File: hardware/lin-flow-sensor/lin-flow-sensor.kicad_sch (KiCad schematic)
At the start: 27 parts, among them J1 UPDI, J2 I2C LCD, J3 Screw_Terminal_01x03, Q1 2N7002, Q2 2N7002, U1 TJA1021T, U2 ATtiny824-X, U3 PCA9536DP

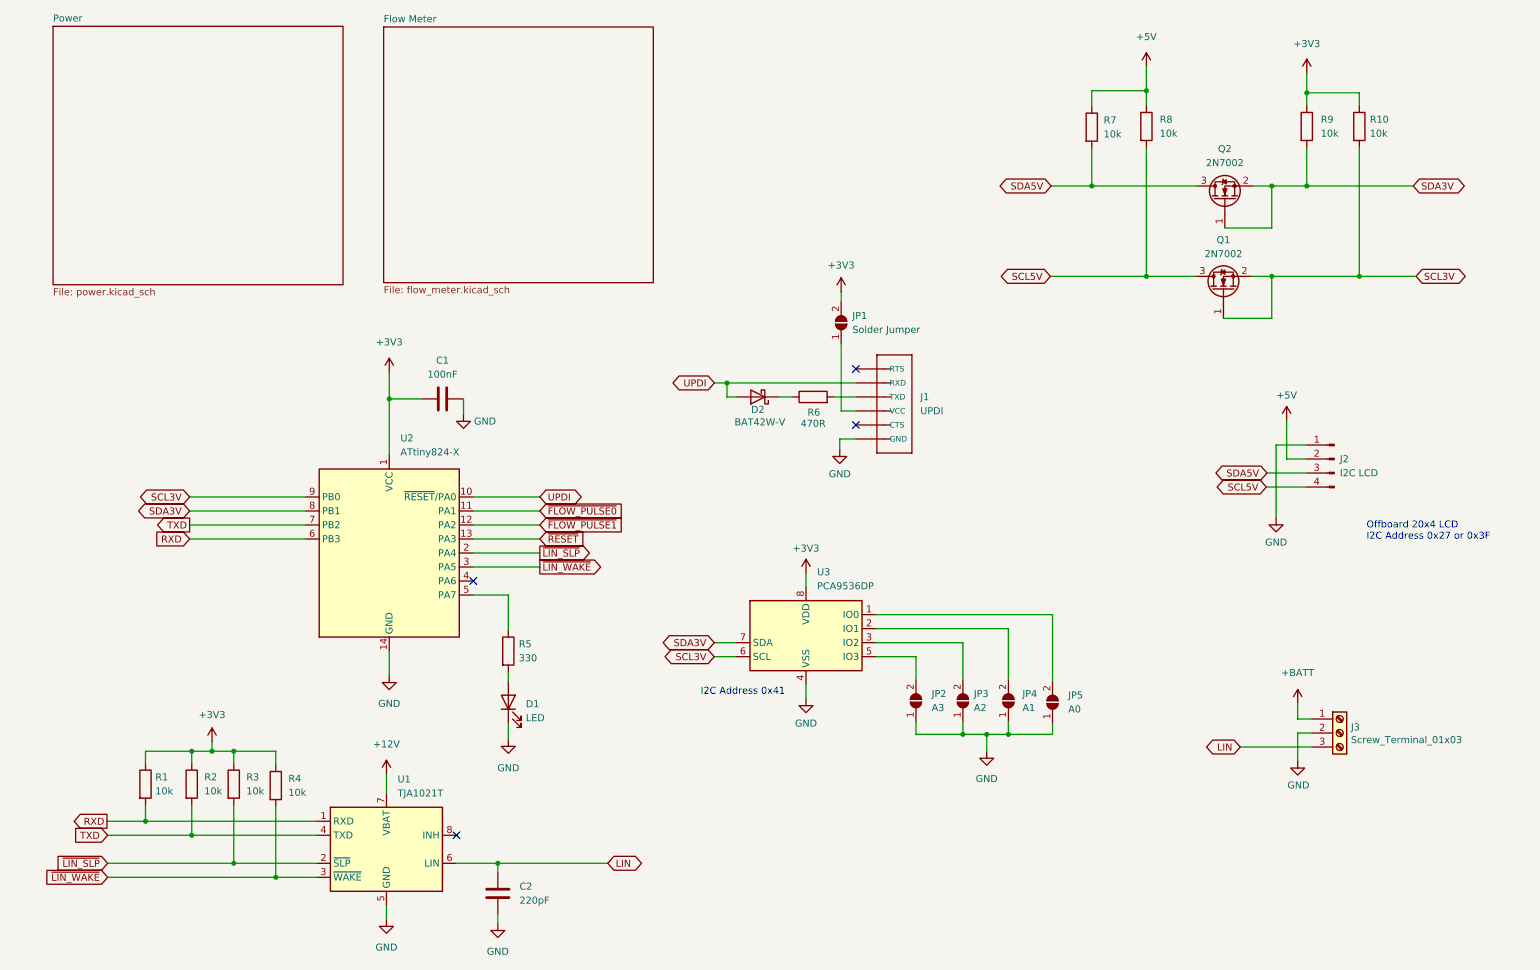
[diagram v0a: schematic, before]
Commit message: Update the schematics... remove PCA9536, use voltage regulator
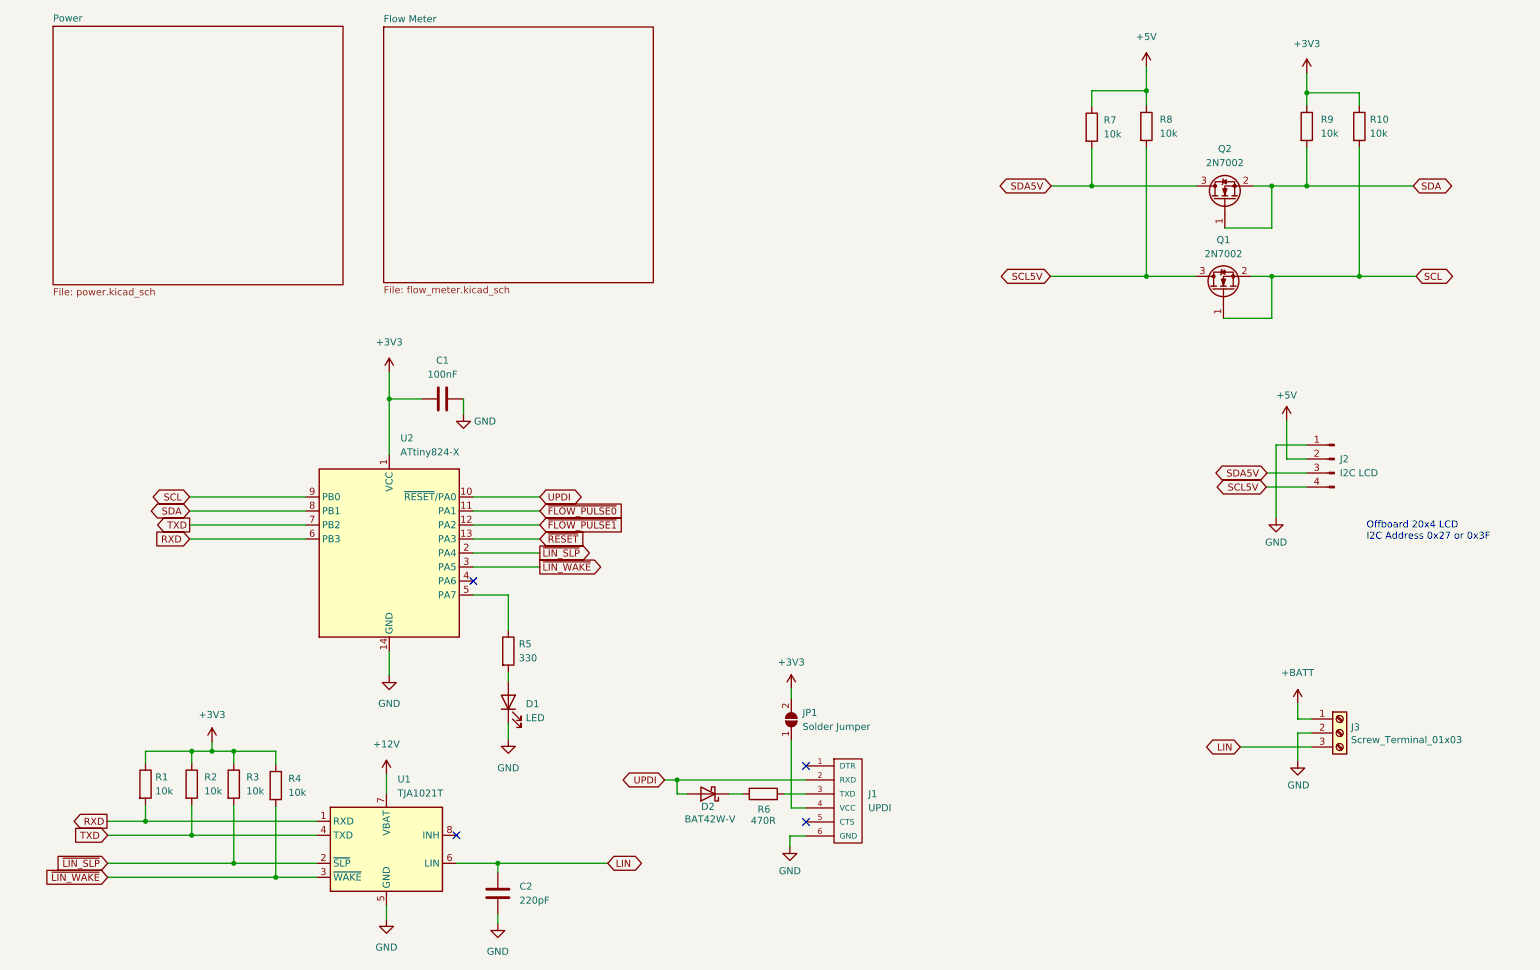
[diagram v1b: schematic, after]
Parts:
- removed JP2: A3, Jumper:SolderJumper-2_P1.3mm_Open_TrianglePad1.0x1.5mm, symbol Jumper:SolderJumper_2_Open
- removed JP3: A2, Jumper:SolderJumper-2_P1.3mm_Open_TrianglePad1.0x1.5mm, symbol Jumper:SolderJumper_2_Open
- removed JP4: A1, Jumper:SolderJumper-2_P1.3mm_Open_TrianglePad1.0x1.5mm, symbol Jumper:SolderJumper_2_Open
- removed JP5: A0, Jumper:SolderJumper-2_P1.3mm_Open_TrianglePad1.0x1.5mm, symbol Jumper:SolderJumper_2_Open
- removed U3: PCA9536DP, Package_SO:TSSOP-8_3x3mm_P0.65mm, symbol Interface_Expansion:PCA9536DP
- J1: footprint Beirdo:FTDI_BASIC -> Beirdo:FTDI-TARGET; symbol Beirdo:FTDI_BASICPTH -> Beirdo:FTDI-TARGET
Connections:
- net GND: now also J1.6 (GND); no longer J1.1 (GND)
- net UPDI: now also J1.2 (RXD); no longer J1.5 (RXD)
- net at J1.3 (TXD): now also R6.2; no longer JP1.1 (A)
- net at J1.4 (VCC): now also JP1.1 (A); no longer R6.2
- net SCL3V renamed SCL
- net SDA3V renamed SDA
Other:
- note removed: "I2C Address 0x41"
- moved on the sheet: D2, JP1, R6
